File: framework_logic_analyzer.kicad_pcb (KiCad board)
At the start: 4 copper layers, 54 x 43 mm, 112 parts, among them IC1 TXU0104QWBQARQ1, IC2 TXU0104QWBQARQ1, IC3 TXU0104QWBQARQ1, IC4 TXU0104QWBQARQ1, IC5 CYUSB3014-BZXC, J3 Conn_ARM_JTAG_SWD_10, J4 6101XX249121_610108249121, J5 6101XX249121_610108249121, J6 6101XX249121_610108249121, J7 6101XX249121_610108249121, P1 USB_C_Receptacle, Q1 MMBT3904, Q2 MMBT3904, Q3 MMBT3904, U1 NCP360SNT1G, U3 AP2112K-3.3, U4 SC189CSKTRT, U5 M24M02-DR, U6 HD3SS3220IRNHT, Y1 19.200 MHz

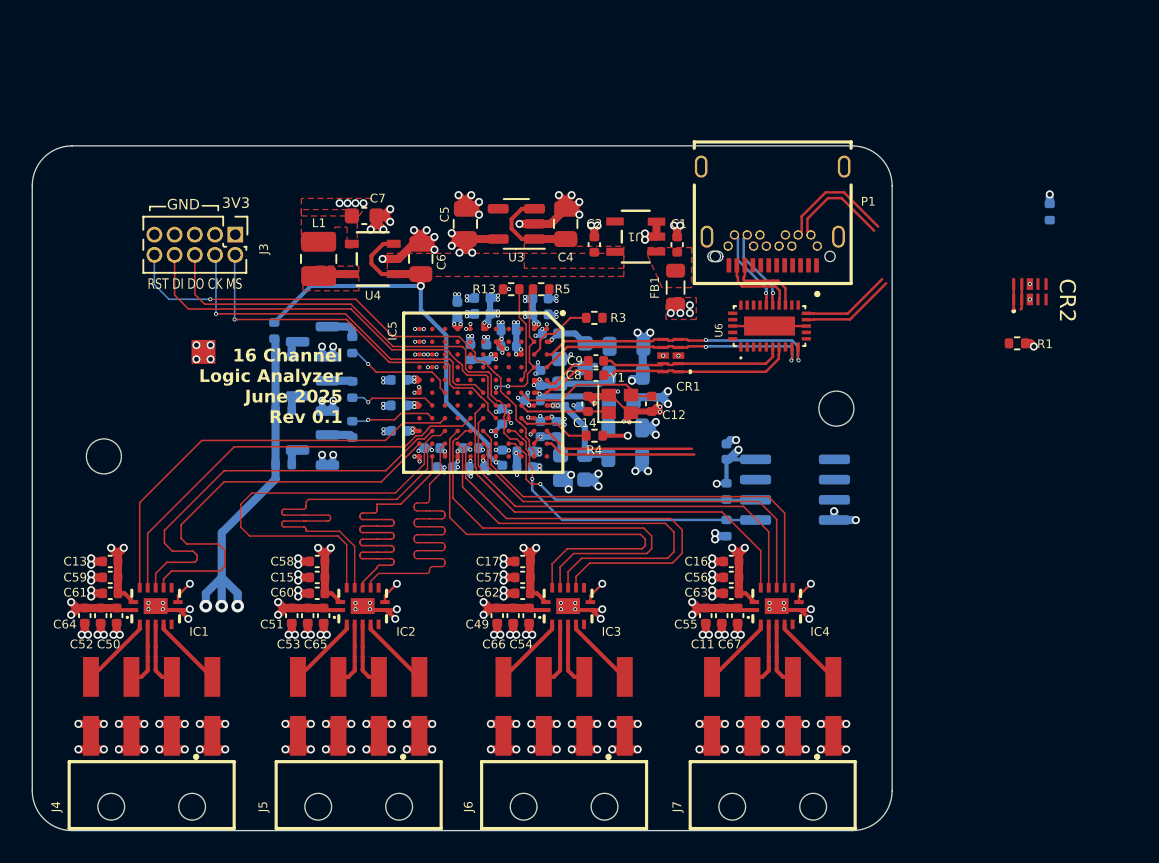
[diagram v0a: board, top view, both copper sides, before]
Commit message: change usb c plug
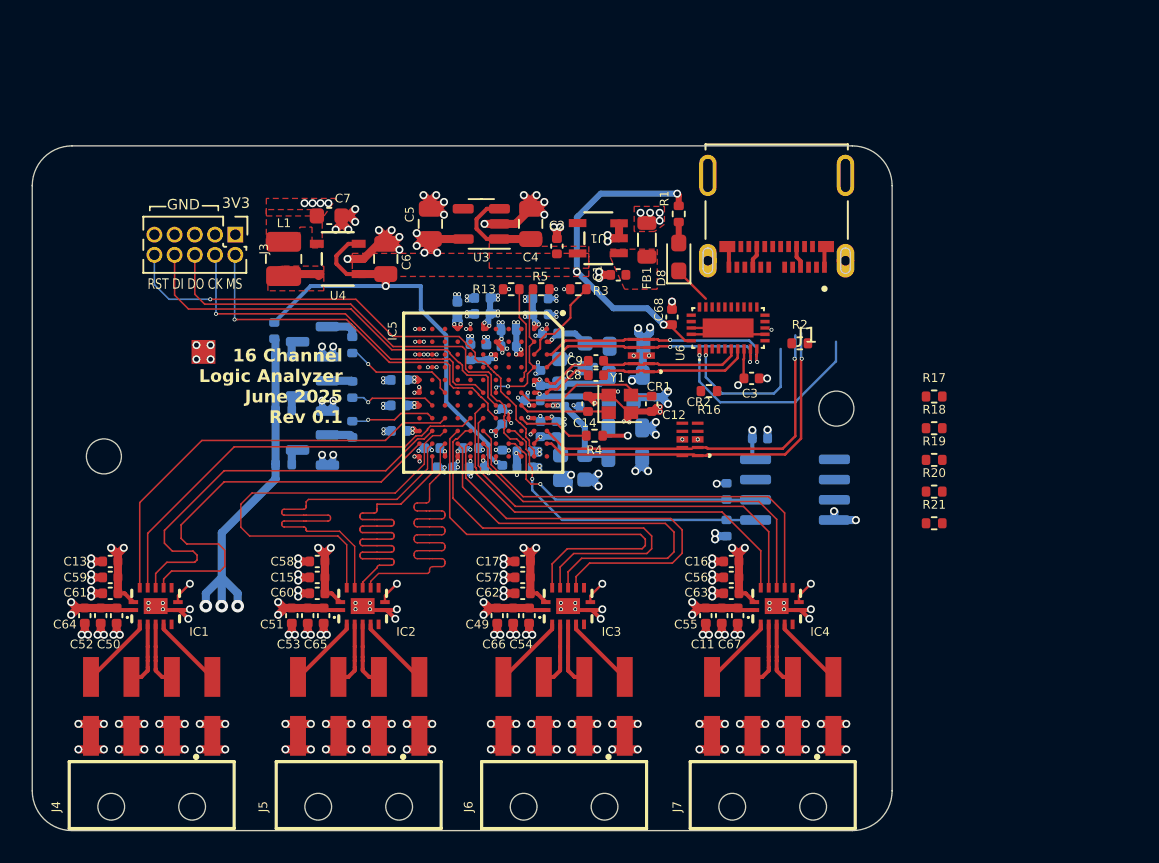
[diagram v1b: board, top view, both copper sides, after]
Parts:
- removed P1: USB_C_Receptacle, Snapeda:USB4056-03-A_REVA2_GCT_USB4056-03-A_REVA2
- added C3: 1u, Capacitor_SMD:C_0402_1005Metric, F.Cu at (154.6, 77.7)
- added C68: 1u, Capacitor_SMD:C_0402_1005Metric, F.Cu at (149.6, 73.8)
- added D8: 150060BS73220, LED_SMD:LED_0603_1608Metric_Pad1.05x0.95mm_HandSolder, F.Cu at (150.0, 70.1)
- added J1: 10152803-00011LF, Snapeda:10152803-00011LF_AMPHENOL_10152803-00011LF, F.Cu at (156.2, 65.0)
- added R16: 900k, Resistor_SMD:R_0402_1005Metric, F.Cu at (151.9, 78.5)
- added R17: 200k, Resistor_SMD:R_0402_1005Metric, F.Cu at (166.0, 78.8)
- added R18: 4k7, Resistor_SMD:R_0402_1005Metric, F.Cu at (166.0, 80.8)
- added R19: 200k, Resistor_SMD:R_0402_1005Metric, F.Cu at (166.0, 82.8)
- added R20: 200k, Resistor_SMD:R_0402_1005Metric, F.Cu at (166.0, 84.8)
- added R21: 200k, Resistor_SMD:R_0402_1005Metric, F.Cu at (166.0, 86.8)
- R1: value 5.1k -> 10k
- R2: value 5.1k -> 200k; moved to F.Cu
- moved CR2 23.3 mm to (150.7, 81.5), turned to 180 degrees
- moved R1 22.8 mm to (150.0, 67.4), turned to 90 degrees
- moved R2 17.7 mm to (157.6, 75.5), turned to 0 degrees
- moved C1 4.16 mm to (146.2, 71.2), turned to 180 degrees
- moved FB1 3.50 mm to (148.0, 69.0), turned to -90 degrees
- moved U6 2.60 mm to (153.1, 74.5)
- moved U1 2.35 mm to (144.9, 68.9)
- moved C2 2.35 mm to (142.3, 69.4)
- moved C48 2.26 mm to (155.1, 81.5), turned to 0 degrees
- moved C4 2.20 mm to (140.7, 68.0)
- moved C6 2.20 mm to (131.6, 70.2)
- moved U3 2.20 mm to (137.6, 68.0)
- moved C5 2.20 mm to (134.4, 68.0)
- moved C7 2.20 mm to (128.1, 67.5)
- moved L1 2.20 mm to (125.2, 70.2)
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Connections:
- CR2 pad 1: /USB-C/SSD+ -> /USB-C/SSD-
- CR2 pad 10: /USB-C/SSD+ -> /USB-C/SSD-
- CR2 pad 2: /USB-C/SSD- -> /USB-C/SSD+
- CR2 pad 9: /USB-C/SSD- -> /USB-C/SSD+
- R1 pad 1: unconnected-(R1-Pad1) -> Net-(D8-A)
- R1 pad 2: GND -> VBUS
- R2 pad 1: unconnected-(R2-Pad1) -> Net-(U6-DIR)
- R2 pad 2: GND -> VBUS
- U6 pad 11: unconnected-(U6-DIR-Pad11) -> Net-(U6-DIR)
- U6 pad 12: unconnected-(U6-~{ENN_MUX}-Pad12) -> GND
- U6 pad 23: unconnected-(U6-~{INT_N}/OUT3-Pad23) -> Net-(U6-~{INT_N}/OUT3)
- U6 pad 24: unconnected-(U6-VCONN_FAULT_N-Pad24) -> Net-(D8-K)
- U6 pad 25: unconnected-(U6-SDA/OUT1-Pad25) -> Net-(U6-SDA/OUT1)
- U6 pad 26: unconnected-(U6-SCL/OUT2-Pad26) -> Net-(U6-SCL/OUT2)
- U6 pad 27: unconnected-(U6-ID-Pad27) -> Net-(U6-ID)
- U6 pad 29: unconnected-(U6-~{ENN_CC}-Pad29) -> GND
- U6 pad 30: unconnected-(U6-VDD5-Pad30) -> VBUS
- U6 pad 4: unconnected-(U6-PORT-Pad4) -> Net-(U6-PORT)
- U6 pad 5: unconnected-(U6-VBUS_DET-Pad5) -> Net-(U6-VBUS_DET)
- U6 pad 8: unconnected-(U6-VCC33-Pad8) -> +3V3
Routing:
- net VBUS: track 36.8 -> 57.0 mm, vias 2 -> 5
- net /USB-C/SS_RX1-: track 13.5 -> 0.00 mm
- net /USB-C/CC1: track 0.00 -> 13.5 mm, vias 0 -> 1
- net /USB-C/SS_RX1+: track 12.3 -> 0.00 mm
- net /USB-C/SSD-: track 11.2 -> 23.1 mm, vias 0 -> 1
- net /USB-C/SSD+: track 11.2 -> 22.4 mm, vias 0 -> 1
- net /USB-C/CC2: track 0.00 -> 9.45 mm, vias 0 -> 1
- net GND: track 172.1 -> 177.9 mm, vias 266 -> 269
- net /USB-C/SS_TX2-: track 5.29 -> 0.00 mm, vias 1 -> 0
- net /USB-C/SS_TX2+: track 5.29 -> 0.00 mm, vias 1 -> 0
- net /USB-C/SS_RX2+: track 4.86 -> 0.00 mm
- net /USB-C/SS_RX2-: track 4.84 -> 0.00 mm
- net Net-(FB1-Pad1): track 3.49 -> 0.00 mm
- net /USB-C/VBUS_CON_IN: track 0.00 -> 2.81 mm
- net /USB-C/SS_TX+: track 11.6 -> 8.91 mm
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- added copper zone on In2.Cu, net Net-(FB1-Pad1)

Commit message: implement USB3.0 active redriver and fix DRC errors
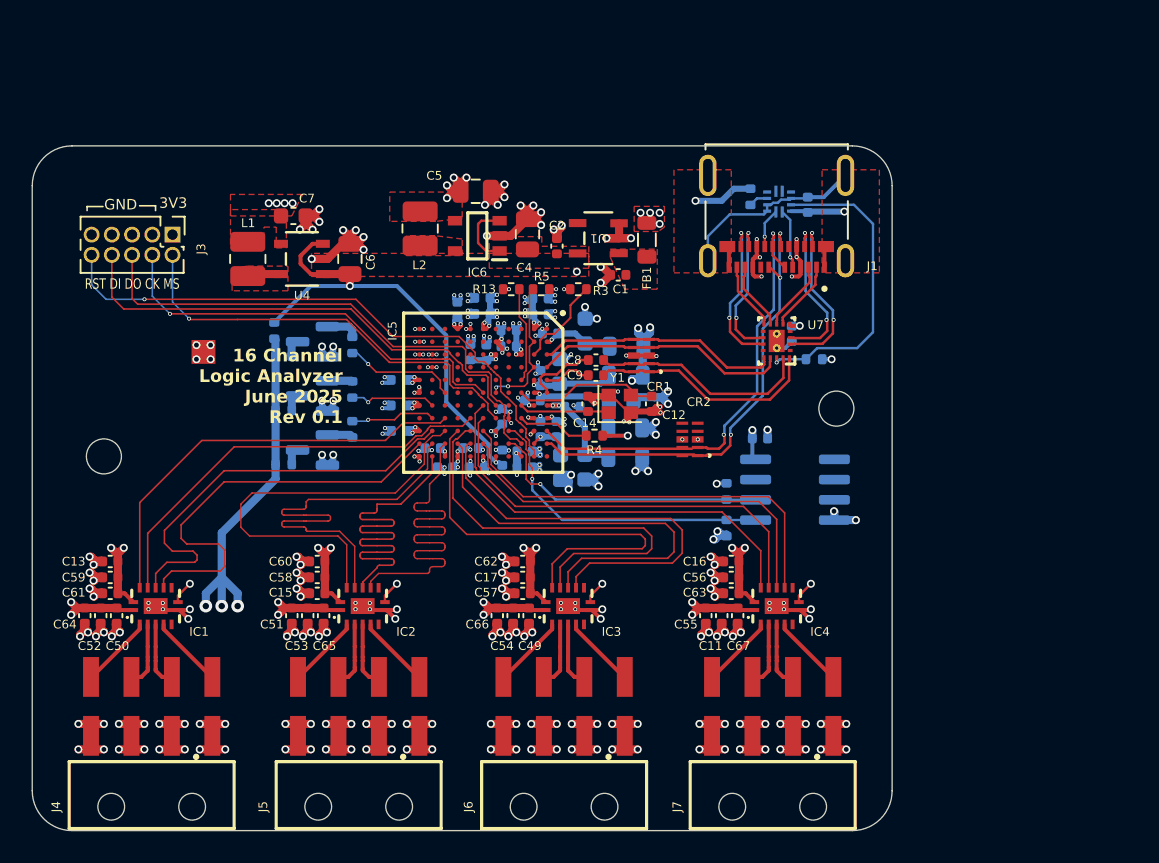
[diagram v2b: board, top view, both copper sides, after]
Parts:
- removed D8: 150060BS73220, LED_SMD:LED_0603_1608Metric_Pad1.05x0.95mm_HandSolder
- removed R16: 900k, Resistor_SMD:R_0402_1005Metric
- removed R17, R19, R20, R21: 200k, Resistor_SMD:R_0402_1005Metric
- removed R18: 4k7, Resistor_SMD:R_0402_1005Metric
- removed U3: AP2112K-3.3, Package_TO_SOT_SMD:SOT-23-5
- removed U6: HD3SS3220IRNHT, Snapeda:HD3SS3220IRNHT_QFN40P450X250X80-31N120X320
- added IC6: XC9285B18CMR-G, Samacsys:SOT95P280X130-5N, F.Cu at (137.3, 68.8)
- added L2: 2.2u, Inductor_SMD:L_1008_2520Metric, F.Cu at (133.8, 68.3)
- added U2: TUSB321RWBR, Snapeda:RWB0012A, B.Cu at (156.3, 66.6)
- added U7: TUSB542RWQR, Snapeda:RWQ0018A, F.Cu at (156.2, 75.3)
- C3, C68: moved to B.Cu
- R1: value 10k -> 900k; moved to B.Cu
- R2: value 200k -> 47k; moved to B.Cu
- moved C68 11.1 mm to (158.1, 66.8)
- moved R1 4.63 mm to (154.5, 66.3)
- moved J3 3.94 mm to (118.2, 68.7)
- moved C3 3.77 mm to (157.1, 74.9), turned to -90 degrees
- moved C5 3.51 mm to (137.2, 66.0), turned to 0 degrees
- moved C7 2.25 mm to (125.8, 67.5)
- moved U4 2.25 mm to (126.3, 70.2)
- moved C6 2.25 mm to (129.3, 70.2)
- moved L1 2.25 mm to (122.9, 70.2)
- moved C49 2.00 mm to (140.6, 92.6)
- moved C60 2.00 mm to (127.3, 89.2)
- moved C62 2.00 mm to (140.2, 89.2)
- moved C21 1.55 mm to (144.1, 74.7), turned to 90 degrees
- moved R2 1.35 mm to (158.5, 76.5)
- moved C15 1.00 mm to (127.3, 91.2)
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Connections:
- C13 pad 1: +3V3 -> +1V8
- C15 pad 1: +3V3 -> +1V8
- C16 pad 1: +3V3 -> +1V8
- C17 pad 1: +3V3 -> +1V8
- C3 pad 1: +3V3 -> +1V8
- C37 pad 1: +3V3 -> +1V8
- C38 pad 1: +3V3 -> +1V8
- C39 pad 1: +3V3 -> +1V8
- C40 pad 1: +3V3 -> +1V8
- C41 pad 1: +3V3 -> +1V8
- C42 pad 1: +3V3 -> +1V8
- C43 pad 1: +3V3 -> +1V8
- C44 pad 1: +3V3 -> +1V8
- C45 pad 1: +3V3 -> +1V8
- C46 pad 1: +3V3 -> +1V8
- C47 pad 1: +3V3 -> +1V8
- C48 pad 1: +3V3 -> +1V8
- C5 pad 1: +3V3 -> +1V8
- C56 pad 1: +3V3 -> +1V8
- C57 pad 1: +3V3 -> +1V8
- C58 pad 1: +3V3 -> +1V8
- C59 pad 1: +3V3 -> +1V8
- C60 pad 1: +3V3 -> +1V8
- C61 pad 1: +3V3 -> +1V8
- C62 pad 1: +3V3 -> +1V8
- C63 pad 1: +3V3 -> +1V8
- CR1 pad 1: /USB-C/SS_TX- -> /USB-C/SS_TX+
- CR1 pad 10: /USB-C/SS_TX- -> /USB-C/SS_TX+
- CR1 pad 2: /USB-C/SS_TX+ -> /USB-C/SS_TX-
- CR1 pad 9: /USB-C/SS_TX+ -> /USB-C/SS_TX-
- FB1 pad 1: Net-(FB1-Pad1) -> /USB-C/VBUS_CON_IN
- FB4 pad 2: +3V3 -> +1V8
- IC1 pad 14: +3V3 -> +1V8
- IC1 pad 8: +3V3 -> +1V8
- IC2 pad 14: +3V3 -> +1V8
- IC2 pad 8: +3V3 -> +1V8
- IC3 pad 14: +3V3 -> +1V8
- IC3 pad 8: +3V3 -> +1V8
- IC4 pad 14: +3V3 -> +1V8
- IC4 pad 8: +3V3 -> +1V8
- IC5 pad B1: +3V3 -> +1V8
- IC5 pad C11: +3V3 -> +1V8
- IC5 pad E3: +3V3 -> +1V8
- IC5 pad F1: +3V3 -> +1V8
- IC5 pad H11: +3V3 -> +1V8
- IC5 pad L9: +3V3 -> +1V8
- J3 pad 1: +3V3 -> +1V8
- R13 pad 1: +3V3 -> +1V8
- R14 pad 1: +3V3 -> +1V8
- R15 pad 1: +3V3 -> +1V8
- R2 pad 1: Net-(U6-DIR) -> /USB-C/USB_FLIPPER
- R2 pad 2: VBUS -> +1V8
- U5 pad 8: +3V3 -> +1V8
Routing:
- net +3V3: track 65.3 -> 0.00 mm, vias 46 -> 0
- net +1V8: track 0.00 -> 58.9 mm, vias 0 -> 47
- net GND: track 177.9 -> 199.1 mm, vias 269 -> 267
- net /USB-C/USB_FLIPPER: track 0.00 -> 19.6 mm, vias 0 -> 1
- net /USB-C/SS_RX1+: track 0.00 -> 10.8 mm, vias 0 -> 2
- net /USB-C/SS_RX1-: track 0.00 -> 10.2 mm, vias 0 -> 2
- net /USB-C/SS_TX2+: track 0.00 -> 9.88 mm, vias 0 -> 2
- net /USB-C/CC1: track 13.5 -> 3.74 mm
- net /USB-C/SS_TX2-: track 0.00 -> 9.28 mm, vias 0 -> 2
- net /USB-C/CC2: track 9.45 -> 2.46 mm
- net /USB-C/SSD+: track 22.4 -> 28.4 mm, vias 1 -> 2
- net /USB-C/SS_TX+: track 8.91 -> 14.6 mm
- net /USB-C/SSD-: track 23.1 -> 28.4 mm, vias 1 -> 3
- net VBUS: track 57.0 -> 62.0 mm
- net /USB-C/SS_TX1+: track 0.00 -> 4.46 mm
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- added copper zone on F.Cu, net +1V8
- added copper zone on In2.Cu, net +1V8
- added copper zone on F.Cu, net /USB-C/VBUS_CON_IN
- added copper zone on In2.Cu, net /USB-C/VBUS_CON_IN
- added copper zone on F.Cu, net GND
- added copper zone on F.Cu, net Net-(IC6-Lx)
- removed copper zone on In2.Cu, net +3V3
- removed copper zone on F.Cu, net Net-(FB1-Pad1)
- removed copper zone on In2.Cu, net Net-(FB1-Pad1)

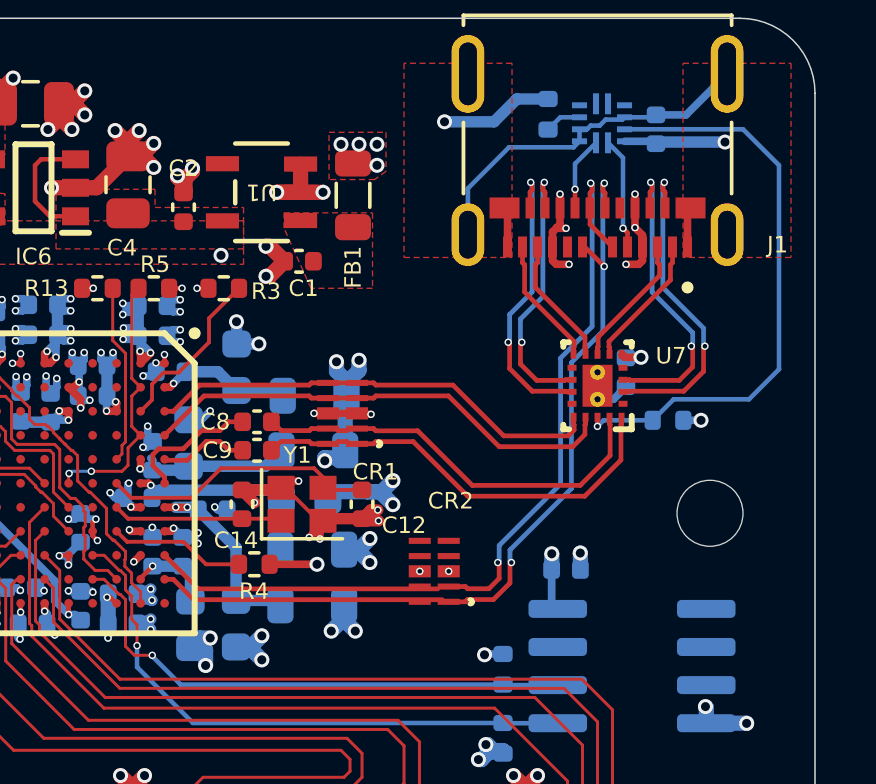
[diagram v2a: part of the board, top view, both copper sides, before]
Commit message: add USB time matching
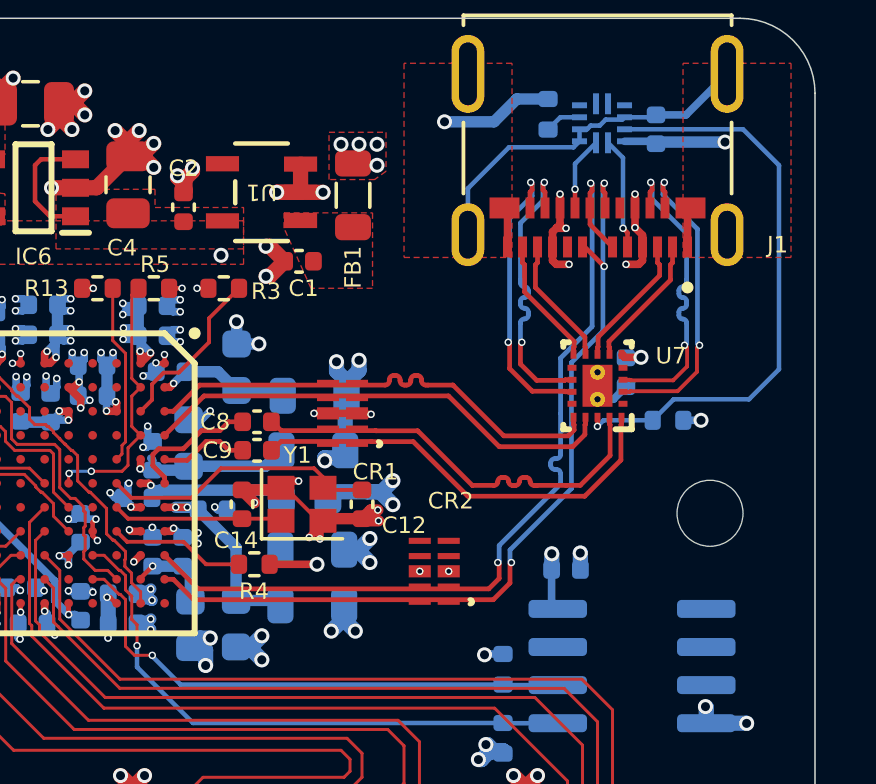
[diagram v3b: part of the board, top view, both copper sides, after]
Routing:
- net /USB-C/SSD+: track 28.4 -> 29.2 mm
- net /USB-C/SS_RX-: track 15.3 -> 16.0 mm
- net /USB-C/SS_TX2-: track 9.28 -> 9.83 mm
